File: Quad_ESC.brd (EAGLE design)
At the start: 96.5 x 40.1 mm, 30 parts, among them J1 SAMTEC-CLT-106-01-X-DJ, J2 SAMTEC-CLT-106-01-X-DJ, J3 SAMTEC-CLT-106-01-X-DJ, Y1 ECS-80-S-4X

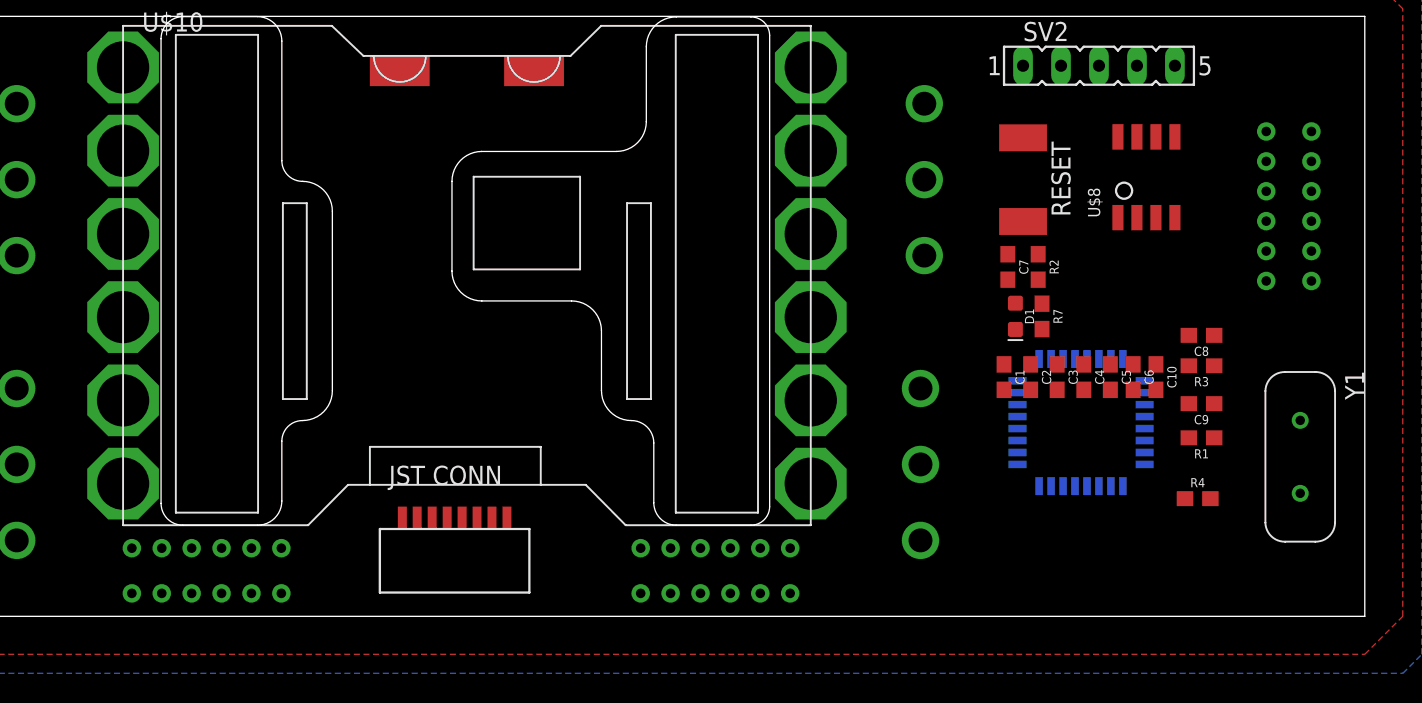
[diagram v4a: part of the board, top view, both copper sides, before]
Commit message: Connector Update!!
made new part for backplae connectors with proper spacing, updated schematic and board accordingly
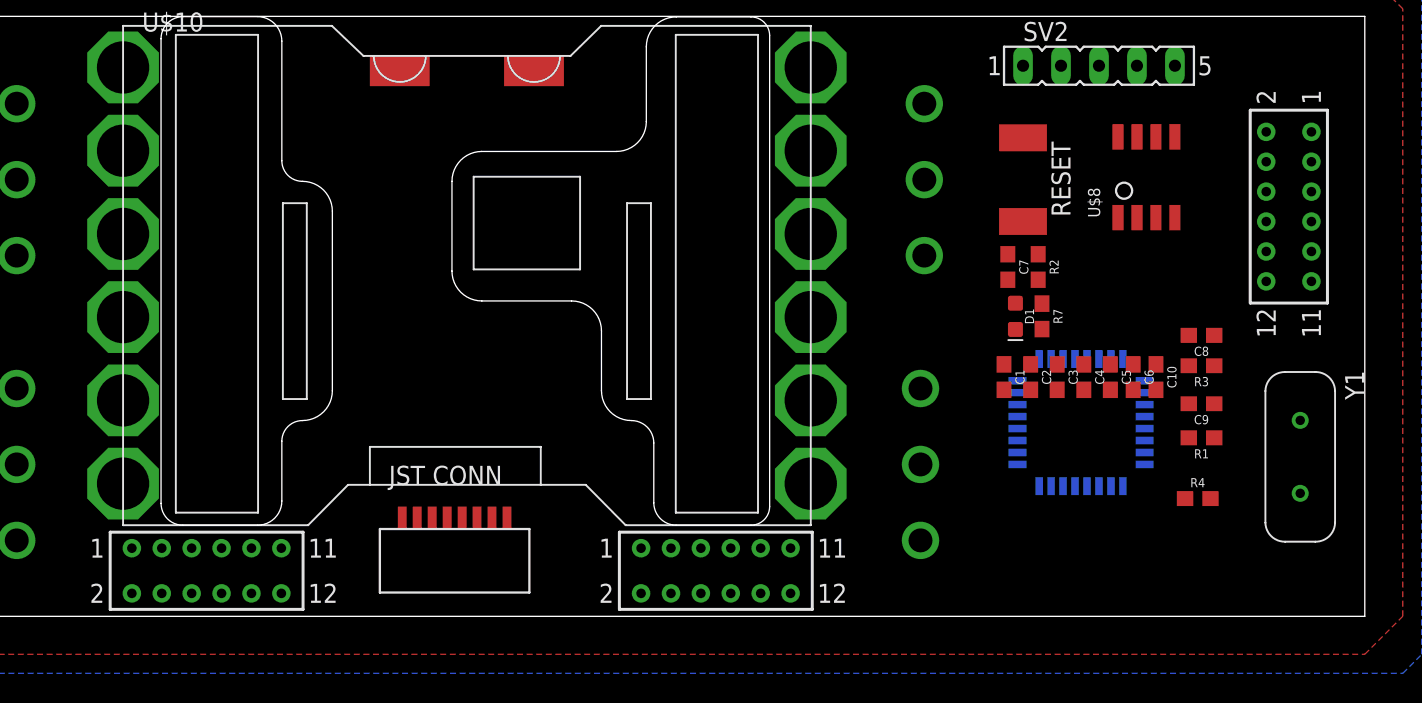
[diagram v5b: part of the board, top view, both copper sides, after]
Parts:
- removed J1, J2, J3: SAMTEC-CLT-106-01-X-DJ, BLHeli_32 45A:SAMTEC-CLT-106-01-X-D
- added U$3: BACKPLANE_CONNECTORS, BLHeli_32 45A:BACKPLANE_CONNECTORS
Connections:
- net +12V: now also U$3.1, U$3.13, U$3.14, U$3.15, U$3.16, U$3.17, U$3.18, U$3.19, U$3.2, U$3.20, U$3.3, U$3.4, U$3.5, U$3.6, U$3.7, U$3.8; no longer J1.1, J1.2, J1.3, J1.4, J1.5, J1.6, J1.7, J1.8, J2.1, J2.2, J2.3, J2.4, J2.5, J2.6, J2.7, J2.8
- net +3V3: now also U$3.25, U$3.26, U$3.27, U$3.28; no longer J3.1, J3.2, J3.3, J3.4
- net CAN_H: now also U$3.29; no longer J3.7
- net CAN_L: now also U$3.31; no longer J3.9
- net GND: now also U$3.10, U$3.11, U$3.12, U$3.21, U$3.22, U$3.23, U$3.24, U$3.9; no longer J1.10, J1.11, J1.12, J1.9, J2.10, J2.11, J2.12, J2.9

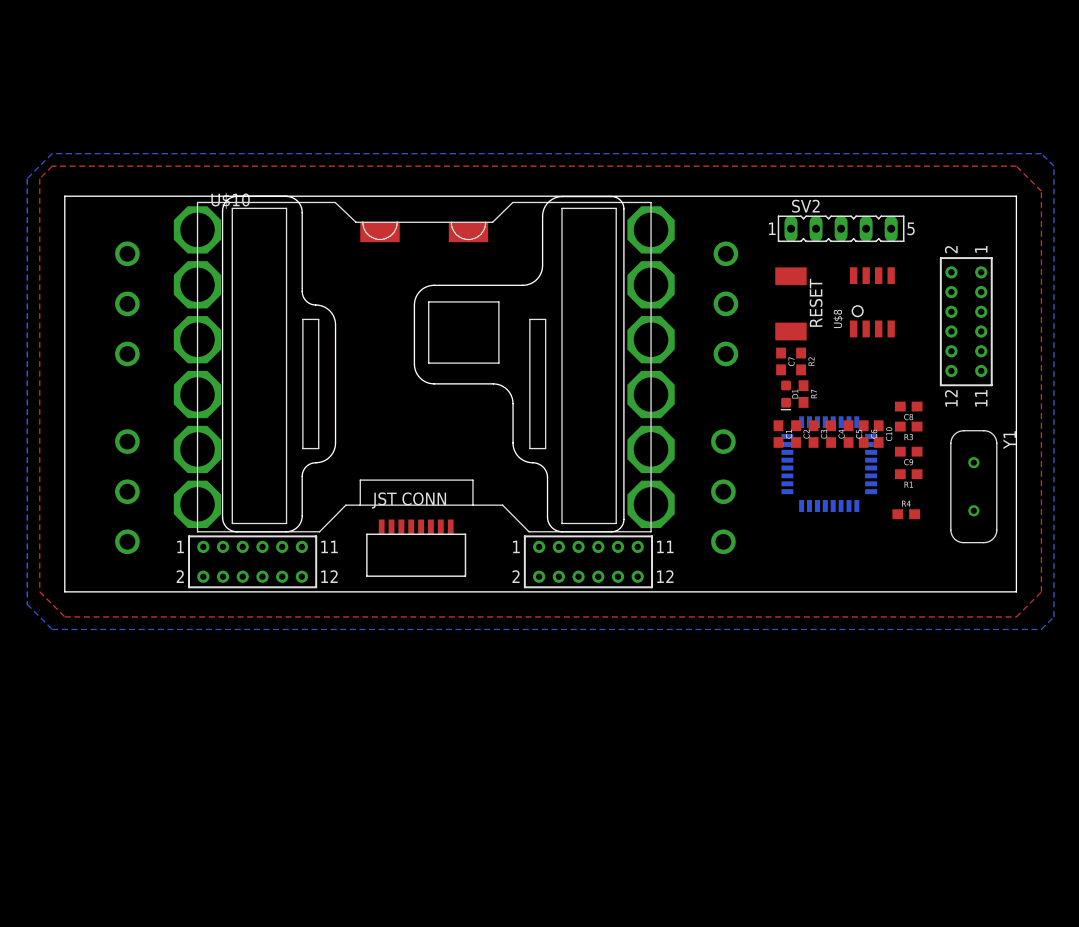
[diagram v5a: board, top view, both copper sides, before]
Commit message: Connector Updates, Board Routing
Backplane connectors updated, board routing on right side completed
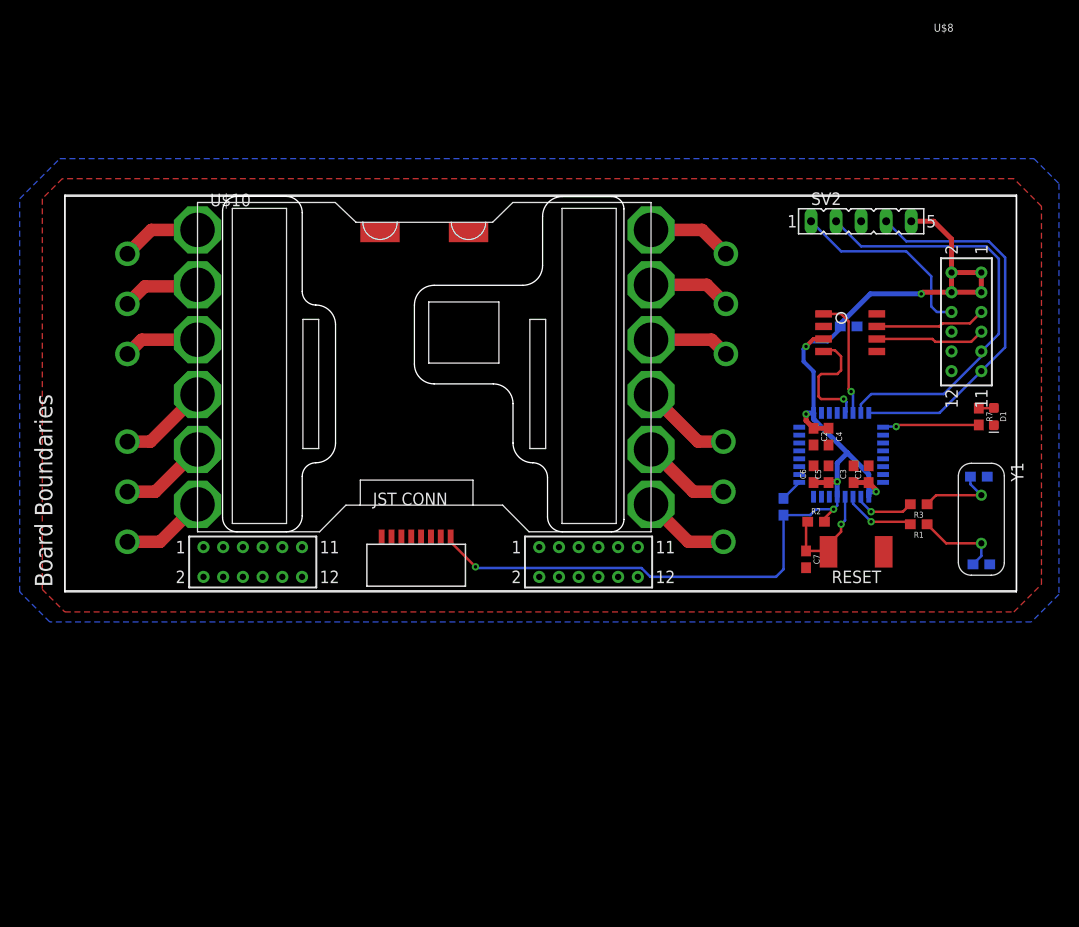
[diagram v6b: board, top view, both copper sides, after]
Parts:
- moved RESET 26.0 mm to (80.3, 4.06), turned to 180 degrees
- moved D1 21.2 mm to (94.2, 17.8)
- moved C7 20.2 mm to (75.2, 3.30)
- moved R7 17.9 mm to (92.7, 17.8)
- moved R2 16.3 mm to (76.2, 7.11), turned to 0 degrees
- moved C9 13.6 mm to (93.0, 2.79), flipped to the bottom
- moved R4 12.5 mm to (72.9, 8.64), flipped to the bottom, turned to 90 degrees
- moved C10 11.3 mm to (79.5, 26.9), flipped to the bottom, turned to 180 degrees
- moved C8 10.1 mm to (92.7, 11.7), flipped to the bottom
- moved C1 10.0 mm to (81.5, 11.9), turned to 90 degrees
- moved R3 7.94 mm to (86.6, 8.89)
- moved U$8 7.23 mm to (77.0, 24.4), turned to 0 degrees
- moved C6 6.51 mm to (75.9, 11.9), turned to 90 degrees
- moved U$4 5.86 mm to (75.9, 9.65), turned to 90 degrees
- moved C3 5.75 mm to (80.0, 11.9), turned to 90 degrees
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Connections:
- removed net 3.3V: R4.1
- new net N$3: R4.2, U$4.PA3
- new net N$7: U$3.32
- new net N$8: U$3.36
- new net TLM: U$2.P$4, U$4.PA5
- net +3V3: now also R4.1, U$2.P$1
- net GND: now also U$2.P$2, U$2.P$3; no longer R4.2, U$4.PA3
- net NRST: now also U$3.30
- net SWCLK: now also U$3.35
- net SWDIO: now also U$3.33
- net TIM3_CH1: now also U$2.P$5
- net TIM3_CH2: now also U$2.P$6
- net TIM3_CH3: now also U$2.P$7
- net TIM3_CH4: now also U$2.P$8
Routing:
- net +3V3: track 0.00 -> 121.2 mm, vias 0 -> 7
- net SWDIO: track 0.00 -> 43.8 mm
- net SWCLK: track 0.00 -> 39.3 mm
- net NRST: track 0.00 -> 19.8 mm
- net CAN_TX: track 0.00 -> 12.3 mm, vias 0 -> 1
- net CAN_RX: track 0.00 -> 12.3 mm, vias 0 -> 1
- net NRST1: track 0.00 -> 12.0 mm, vias 0 -> 1
- net CAN_H: track 0.00 -> 11.2 mm
- net CAN_L: track 0.00 -> 11.1 mm
- net LED: track 0.00 -> 9.81 mm, vias 0 -> 1
- net ESC4_B: track 0.00 -> 9.32 mm
- net ESC2_B: track 0.00 -> 9.09 mm
- net ESC4_R: track 0.00 -> 8.91 mm
- net ESC2_Y: track 0.00 -> 8.89 mm
- net N$1: track 0.00 -> 8.78 mm
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
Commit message: Signals fixed a bit?
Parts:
- moved C5 0.38 mm to (77.1, 11.9)
- moved C6 0.38 mm to (75.6, 11.9)
- moved U$7 0.25 mm to (66.8, 10.4)
- moved C1 0.13 mm to (81.5, 12.1)
- moved C3 0.13 mm to (80.0, 12.1)
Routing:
- net TIM3_CH4: track 0.00 -> 56.3 mm, vias 0 -> 1
- net TIM3_CH3: track 0.00 -> 55.4 mm, vias 0 -> 1
- net TIM3_CH2: track 0.00 -> 54.5 mm, vias 0 -> 1
- net TIM3_CH1: track 0.00 -> 53.7 mm, vias 0 -> 1
- net +3V3: track 121.2 -> 81.4 mm, vias 7 -> 6
- net TLM: track 0.00 -> 9.79 mm, vias 0 -> 1

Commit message: Board Update (again)
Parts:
- moved U$10 0.51 mm to (13.5, 6.60)
- moved U$3 0.25 mm to (19.1, 3.28)
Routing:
- net +12V: track 0.00 -> 129.6 mm, vias 0 -> 1
- net +3V3: track 81.4 -> 140.9 mm, vias 6 -> 9
- net TLM: track 9.79 -> 56.5 mm, vias 1 -> 3
- net ESC1_Y: track 7.34 -> 8.22 mm
- net ESC4_Y: track 8.61 -> 9.43 mm
